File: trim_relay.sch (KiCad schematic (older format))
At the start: 29 parts, among them J1 Conn_01x01, J10 Conn_01x01, J11 Conn_01x01, J12 Conn_01x01, J13 GS2, J14 GS2, J2 Conn_01x01, J3 Conn_01x01, J4 Conn_01x01, J5 Conn_01x01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

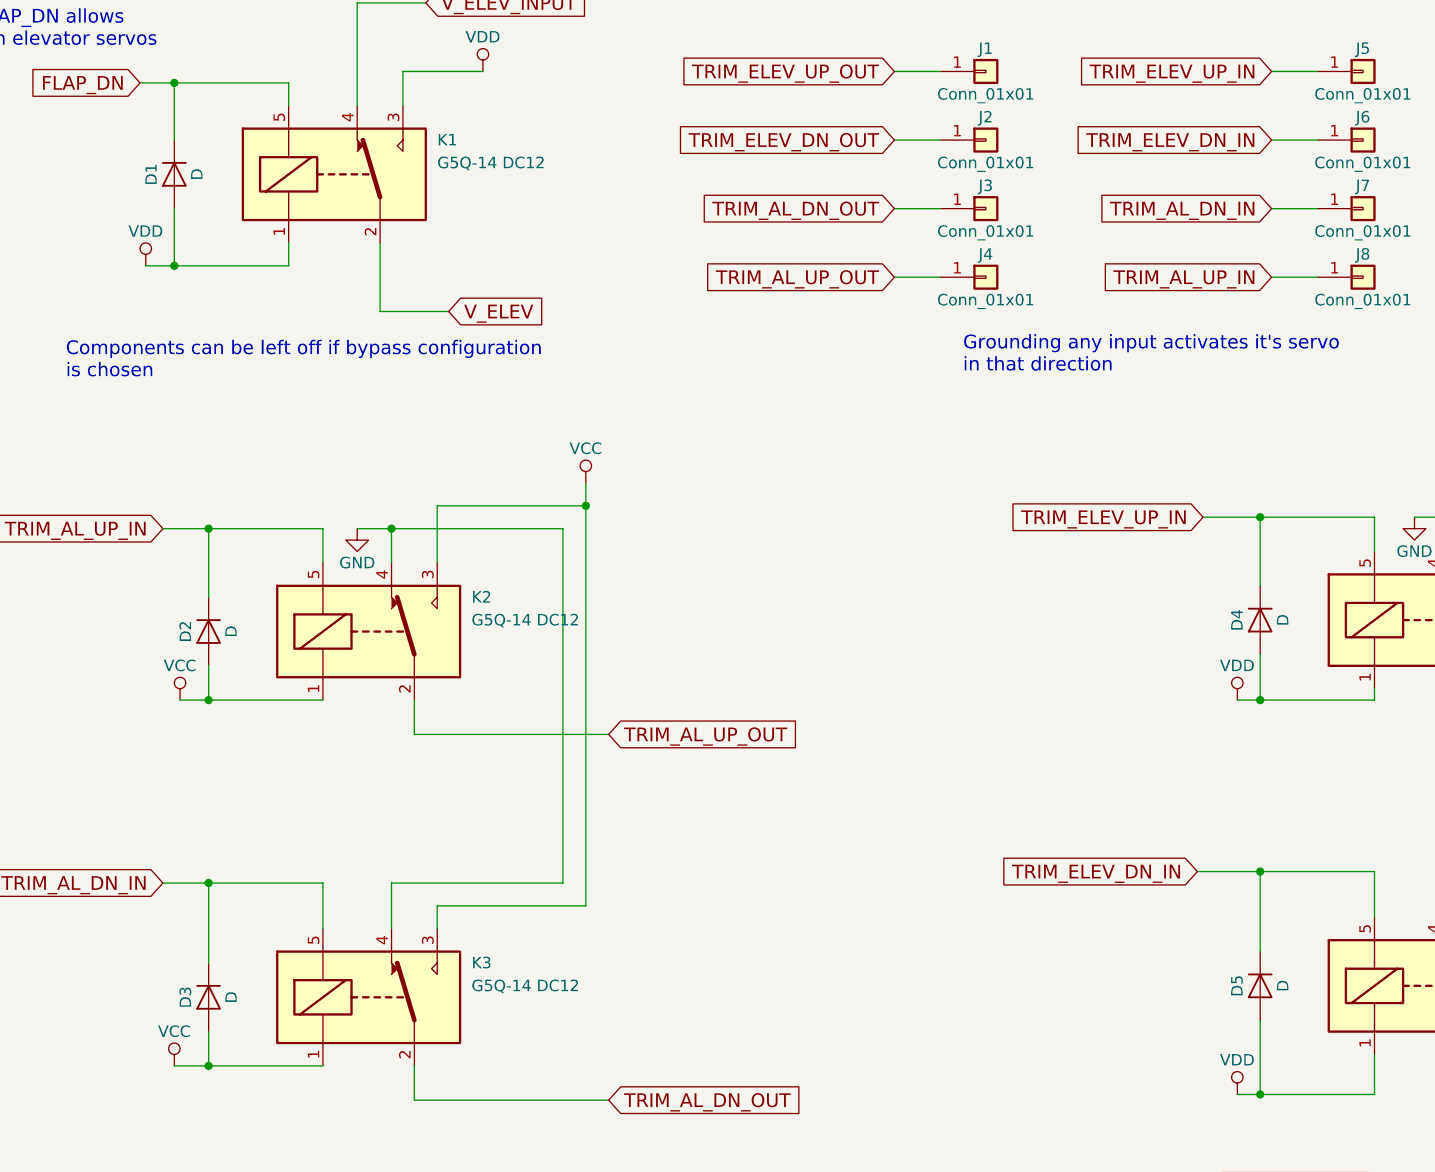
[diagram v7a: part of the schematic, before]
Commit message: Diodes were backwards
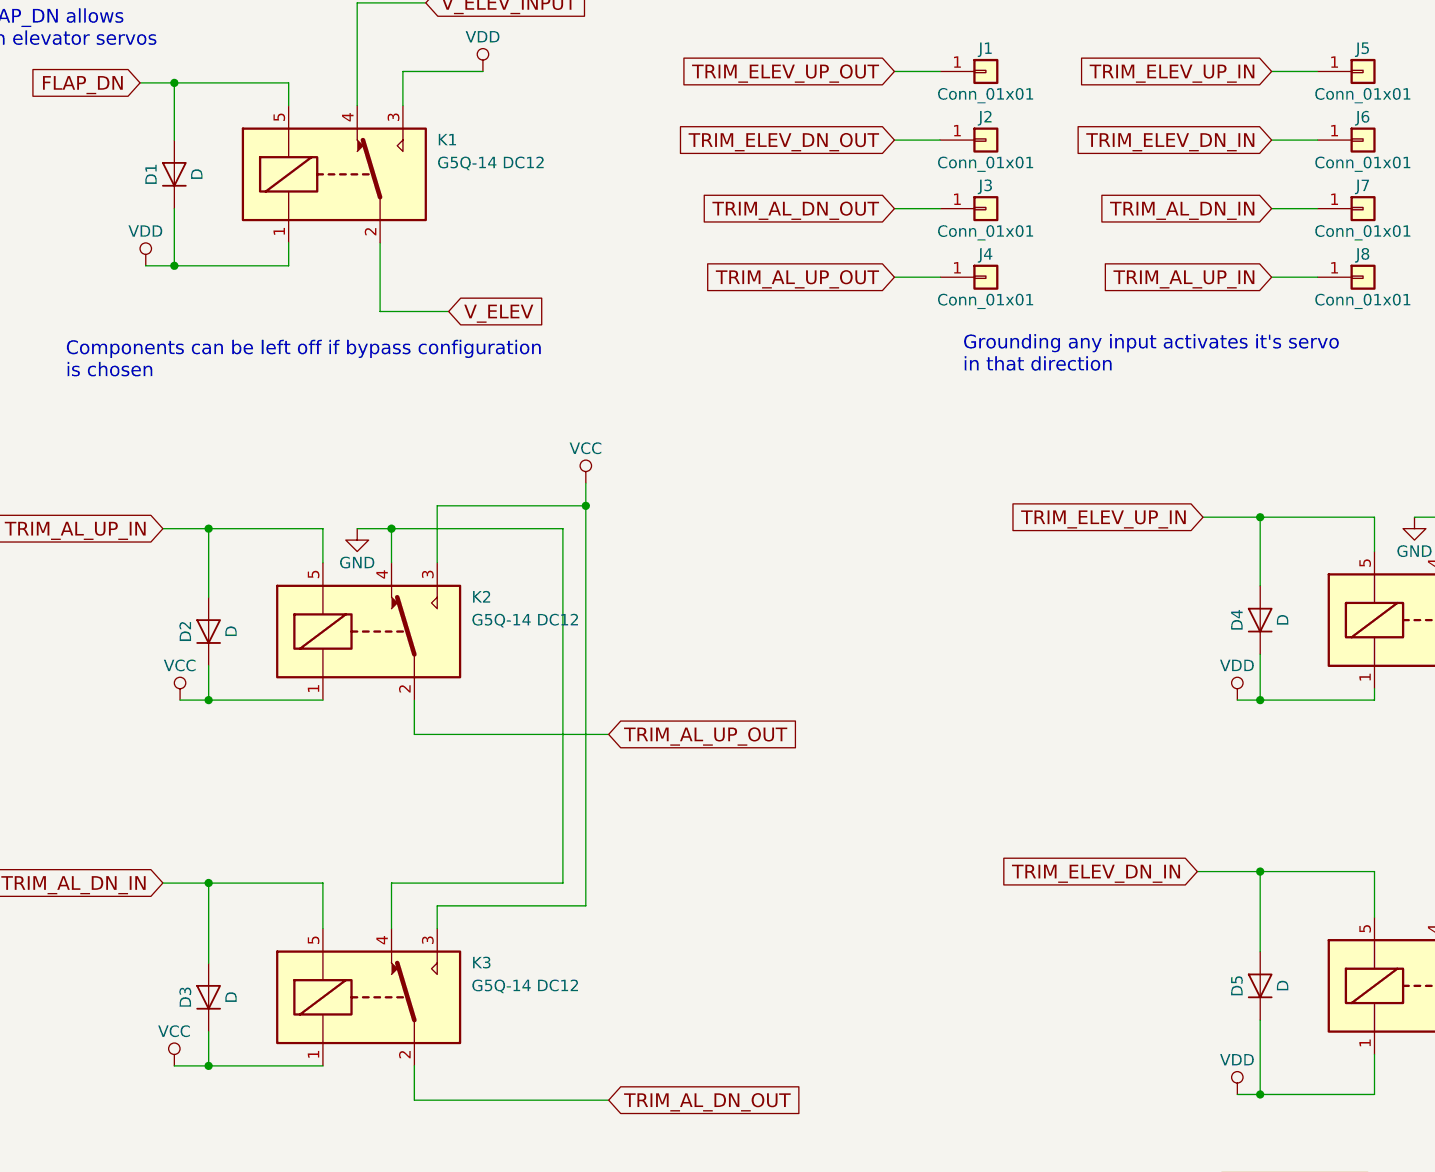
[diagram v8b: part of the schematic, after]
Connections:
- net FLAP_DN: now also D1.2 (A); no longer D1.1 (K)
- net TRIM_AL_DN_IN: now also D3.2 (A); no longer D3.1 (K)
- net TRIM_AL_UP_IN: now also D2.2 (A); no longer D2.1 (K)
- net TRIM_ELEV_DN_IN: now also D5.2 (A); no longer D5.1 (K)
- net TRIM_ELEV_UP_IN: now also D4.2 (A); no longer D4.1 (K)
- net VCC: now also D2.1 (K), D3.1 (K); no longer D2.2 (A), D3.2 (A)
- net VDD: now also D1.1 (K), D4.1 (K), D5.1 (K); no longer D1.2 (A), D4.2 (A), D5.2 (A)
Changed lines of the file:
@@
 Title "RV Trim Relay"
 Date ""
-Rev ""
+Rev "1.1"
 Comp ""
 Comment1 ""
@@
 F 3 "" H 2050 1400 50  0001 C CNN
 	1    2050 1400
-	0    -1   1    0
+	0    -1   -1   0
 $EndComp
 Wire Wire Line
@@
 F 3 "" H 2200 3400 50  0001 C CNN
 	1    2200 3400
-	0    -1   1    0
+	0    -1   -1   0
 $EndComp
 $Comp
@@
 F 3 "" H 2200 5000 50  0001 C CNN
 	1    2200 5000
-	0    -1   1    0
+	0    -1   -1   0
 $EndComp
 Connection ~ 2200 3700
@@
 F 3 "" H 6800 3350 50  0001 C CNN
 	1    6800 3350
-	0    -1   1    0
+	0    -1   -1   0
 $EndComp
 $Comp
@@
 F 3 "" H 6800 4950 50  0001 C CNN
 	1    6800 4950
-	0    -1   1    0
+	0    -1   -1   0
 $EndComp
 Wire Wire Line
